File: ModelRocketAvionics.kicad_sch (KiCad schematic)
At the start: 64 parts, among them P1 USB_C_Plug, Q1 AO3400A, Q2 NCE8205, Q3 AO3400A, SW1 SW_SPDT, U1 ICM-42605, U2 W25Q16JVSS, U3 BMP280, U4 RP2040, U6 L86-M33, U7 915MHz, U9 AP7361C-33E, X1 Crystal_GND24_Small

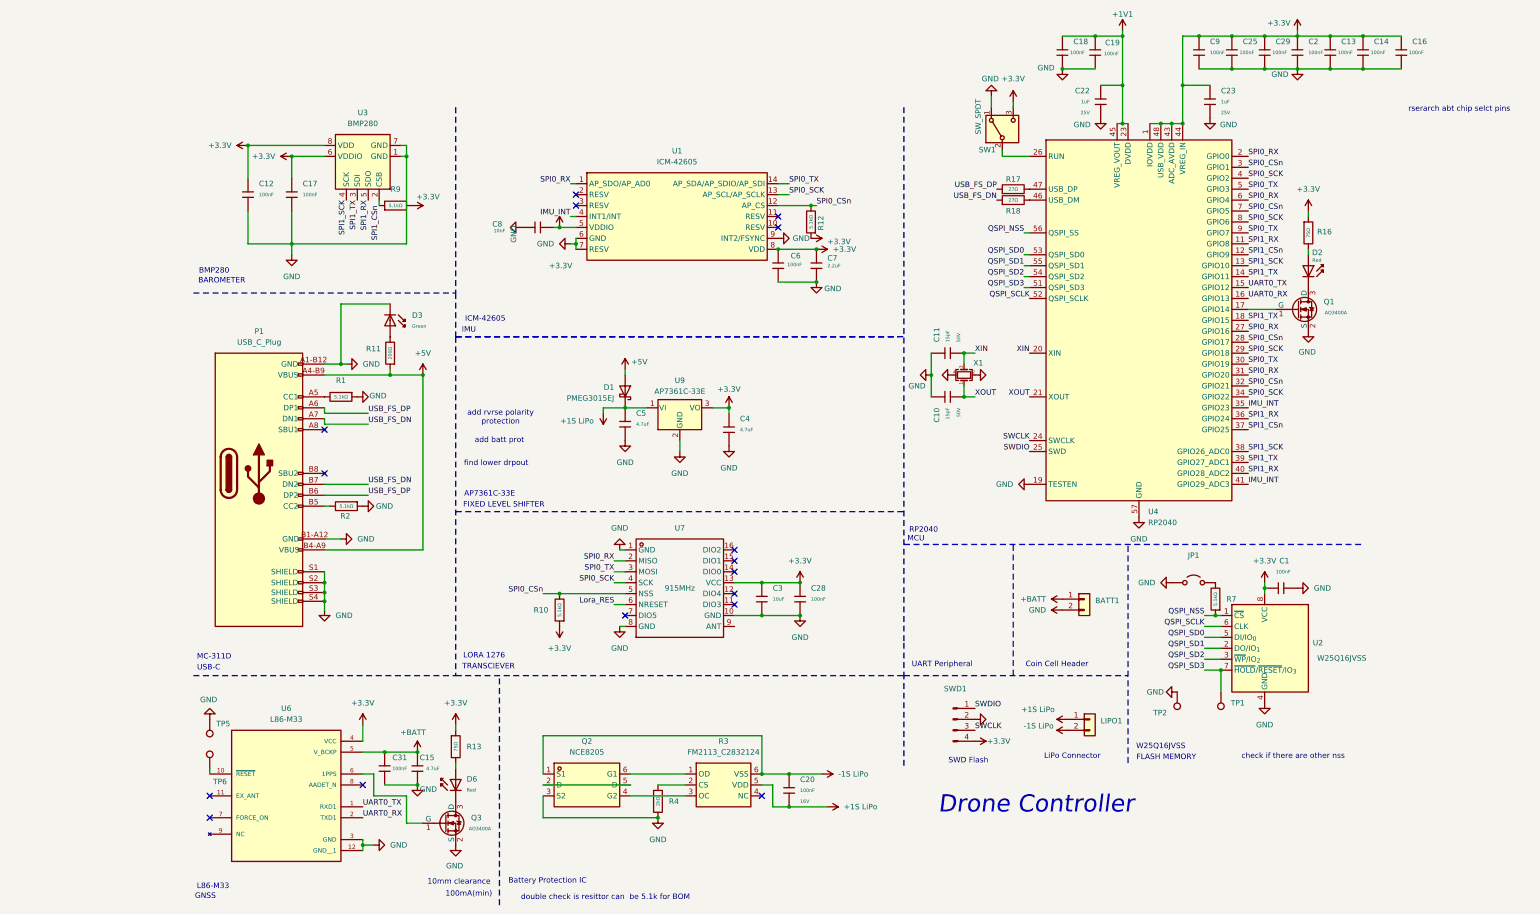
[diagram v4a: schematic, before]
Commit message: Fixed layout of Schematic and pin labelling.
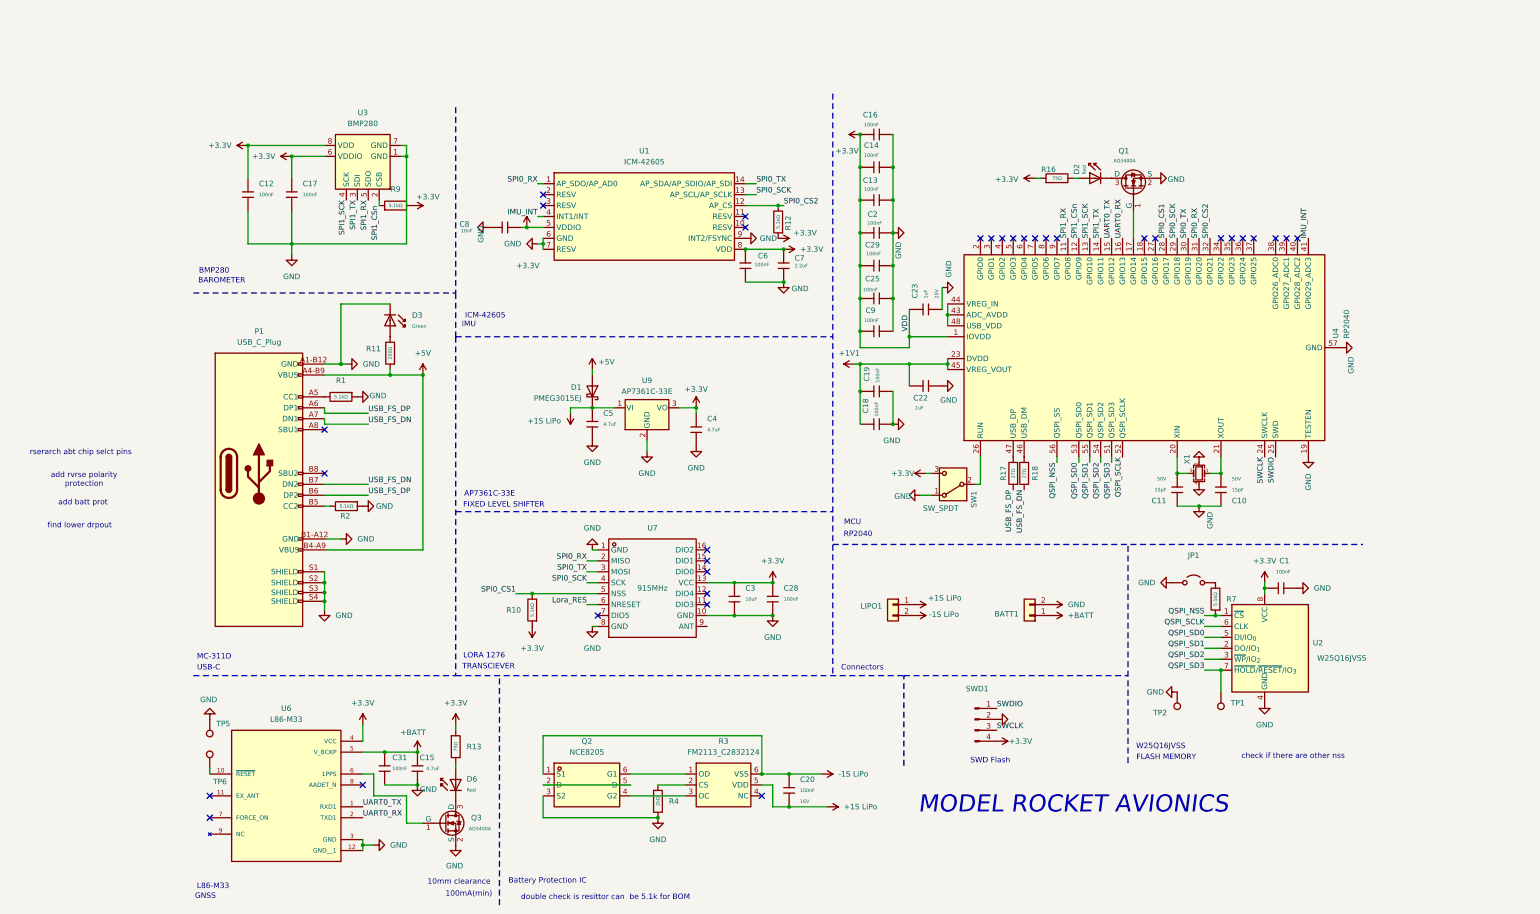
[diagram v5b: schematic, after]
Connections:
- net +3.3V: no longer U4.43 (ADC_AVDD), U4.44 (VREG_IN), U4.48 (USB_VDD)
- net IMU_INT: no longer U4.35 (GPIO23)
- net SPI0_RX: no longer U4.2 (GPIO0), U4.27 (GPIO16), U4.6 (GPIO4)
- net SPI0_SCK: no longer U4.34 (GPIO22), U4.4 (GPIO2), U4.8 (GPIO6)
- net SPI0_TX: no longer U4.5 (GPIO3), U4.9 (GPIO7)
- net SPI1_CSn: no longer U4.37 (GPIO25)
- net SPI1_RX: no longer U4.36 (GPIO24), U4.40 (GPIO28_ADC2)
- net SPI1_SCK: no longer U4.38 (GPIO26_ADC0)
- net SPI1_TX: no longer U4.18 (GPIO15), U4.39 (GPIO27_ADC1)
- removed net SPI0_CSn: R10.2, R12.2, U1.12 (AP_CS), U4.28 (GPIO17), U4.3 (GPIO1), U4.32 (GPIO21), U4.7 (GPIO5), U7.5 (NSS)
- net XIN: no longer names the net of C11.2, U4.20 (XIN), X1.3
- net XOUT: no longer names the net of C10.2, U4.21 (XOUT), X1.1
- new net: U4.43 (ADC_AVDD), U4.44 (VREG_IN), U4.48 (USB_VDD)
- new net SPI0_CS1: R10.2, U4.28 (GPIO17), U7.5 (NSS)
- new net SPI0_CS2: R12.2, U1.12 (AP_CS), U4.32 (GPIO21)
- no-connect marks 16 -> 33
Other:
- note added: "Connectors"
- note added: "MODEL ROCKET AVIONICS"
- note removed: "Coin Cell Header"
- note removed: "Drone Controller"
- note removed: "LiPo Connector"
- note removed: "UART Peripheral"
- moved on the sheet: BATT1, C10, C11, C13, C14, C16, C18, C19, C2, C22, C23, C25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
